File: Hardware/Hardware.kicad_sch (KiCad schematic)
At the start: 0 parts

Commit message: [Ajout] : Ajout du microcontrolleur STM32WB55RG utilisé dans le projet
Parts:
- added U1: STM32WB55RGVx, Package_DFN_QFN:QFN-68-1EP_8x8mm_P0.4mm_EP6.4x6.4mm, symbol MCU_ST_STM32WB:STM32WB55RGVx
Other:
- company: (none) -> PAR KAMDA JONATAN
- title: (none) -> SAFE ROOM SCHEMATIC
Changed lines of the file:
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@@
 	(generator_version "9.0")
 	(paper "A4")
+	(title_block
+		(title "SAFE ROOM SCHEMATIC")
+		(date "2026-05-06")
+		(rev "0.1")
+		(company "PAR KAMDA JONATAN")
+	)
+	(symbol
+		(lib_id "MCU_ST_STM32WB:STM32WB55RGVx")
+		(at 142.24 86.36 0)
+		(unit 1)
+		(exclude_from_sim no)
+		(in_bom yes)
+		(on_board yes)
+		(dnp no)
+		(fields_autoplaced yes)
+		(property "Reference" "U1"
+			(at 146.9233 134.62 0)
+			(effects
+				(font
+					(size 1.27 1.27)
+				)
+				(justify left)
+			)
+		)
+		(property "Value" "STM32WB55RGVx"
+			(at 146.9233 137.16 0)
+			(effects
+				(font
+					(size 1.27 1.27)
+				)
+				(justify left)
+			)
+		)
+		(property "Footprint" "Package_DFN_QFN:QFN-68-1EP_8x8mm_P0.4mm_EP6.4x6.4mm"
+			(at 121.92 132.08 0)
+			(effects
+				(font
+					(size 1.27 1.27)
+				)
+				(justify right)
+				(hide yes)
+			)
+		)
+		(property "Datasheet" "https://www.st.com/resource/en/datasheet/stm32wb55rg.pdf"
+			(at 142.24 86.36 0)
+			(effects
+				(font
+					(size 1.27 1.27)
+				)
+				(hide yes)
+			)
+		)
+		(property "Description" "STMicroelectronics Arm Cortex-M4 MCU, 1024KB flash, 256KB RAM, 64 MHz, 1.71-3.6V, 49 GPIO, VFQFPN68"
+			(at 142.24 86.36 0)
+			(effects
+				(font
+					(size 1.27 1.27)
+				)
+				(hide yes)
+			)
+		)
+		(pin "25"
+		)
+		(pin "32"
+		)
+		(pin "40"
+		)
+		(pin "58"
+		)
+		(pin "22"
+		)
+		(pin "8"
+		)
+		(pin "41"
+		)
+		(pin "2"
+		)
+		(pin "4"
+		)
+		(pin "26"
+		)
+		(pin "30"
+		)
+		(pin "36"
+		)
+		(pin "10"
+		)
+		(pin "45"
+		)
+		(pin "33"
+		)
+		(pin "55"
+		)
+		(pin "28"
+		)
+		(pin "43"
+		)
+		(pin "35"
+		)
+		(pin "1"
+		)
+		(pin "12"
+		)
+		(pin "61"
+		)
+		(pin "37"
+		)
+		(pin "9"
+		)
+		(pin "69"
+		)
+		(pin "24"
+		)
+		(pin "52"
+		)
+		(pin "19"
+		)
+		(pin "62"
+		)
+		(pin "23"
+		)
+		(pin "34"
+		)
+		(pin "63"
+		)
+		(pin "13"
+		)
+		(pin "11"
+		)
+		(pin "42"
+		)
+		(pin "18"
+		)
+		(pin "56"
+		)
+		(pin "44"
+		)
+		(pin "15"
+		)
+		(pin "57"
+		)
+		(pin "38"
+		)
+		(pin "27"
+		)
+		(pin "59"
+		)
+		(pin "60"
+		)
+		(pin "17"
+		)
+		(pin "68"
+		)
+		(pin "3"
+		)
+		(pin "5"
+		)
+		(pin "31"
+		)
+		(pin "50"
+		)
+		(pin "14"
+		)
+		(pin "16"
+		)
+		(pin "20"
+		)
+		(pin "21"
+		)
+		(pin "51"
+		)
+		(pin "54"
+		)
+		(pin "39"
+		)
+		(pin "64"
+		)
+		(pin "65"
+		)
+		(pin "66"
+		)
+		(pin "53"
+		)
+		(pin "67"
+		)
+		(pin "6"
+		)
+		(pin "7"
+		)
+		(pin "48"
+		)
+		(pin "49"
+		)
+		(pin "46"
+		)
+		(pin "29"
+		)
+		(pin "47"
+		)
+		(instances
+			(project ""
+				(path "/ba4846b8-7c71-441f-b11b-b34cbea60d05"
+					(reference "U1")
+					(unit 1)
+				)
+			)
+		)
+	)
 	(sheet_instances
 		(path "/"

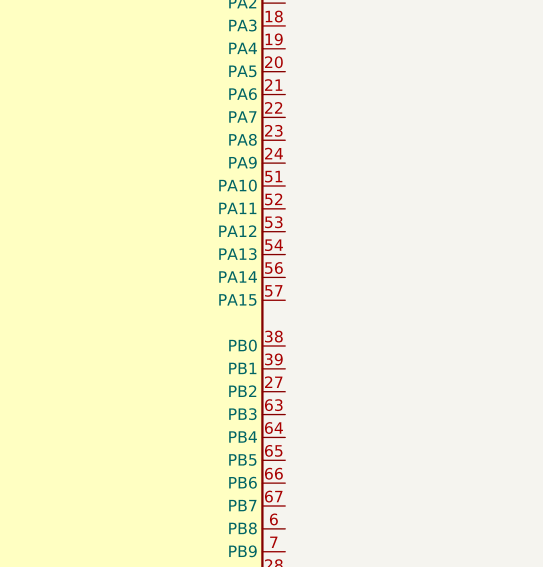
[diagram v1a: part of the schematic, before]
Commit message: [ST-LINK CONNEXION] : Ajout de la connexion ST-LINK pour téléverser le programme finale, il faut une connexion ST-LINK. La pin PA13 c'est pour la data ( SWDIO) La pin PA14 c'est pour l'horloge (SWCLK)
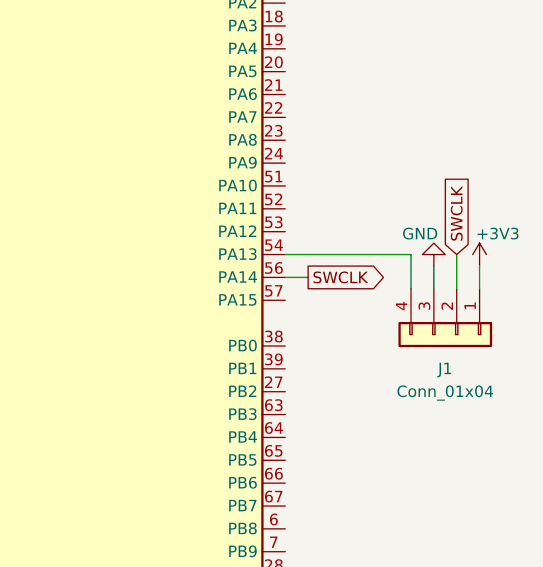
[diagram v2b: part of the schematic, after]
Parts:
- added J1: Conn_01x04, symbol Connector_Generic:Conn_01x04
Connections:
- net at U1.54 (PA13): now also J1.4 (Pin_4)
- net SWCLK: now reaches U1.56 (PA14)
- net SWCLK: now also J1.2 (Pin_2)
- new net +3V3: J1.1 (Pin_1)
- new net GND: J1.3 (Pin_3)

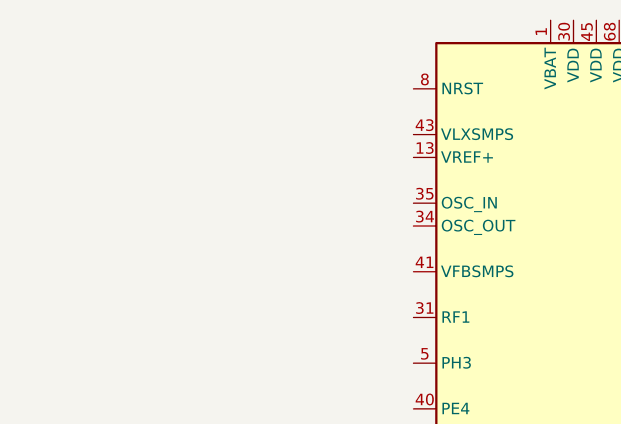
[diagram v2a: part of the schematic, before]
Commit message: [RESET]: Ajout du bouton reset et de la capacité pour filtrer les oscillations du bouton
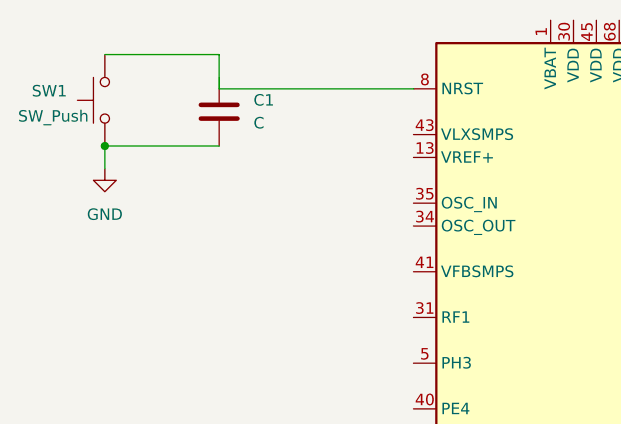
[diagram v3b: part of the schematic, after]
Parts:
- added C1: C, symbol Device:C
- added SW1: SW_Push, symbol Switch:SW_Push
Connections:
- net GND: now also C1.2, SW1.1
- net at U1.8 (NRST): now also SW1.2

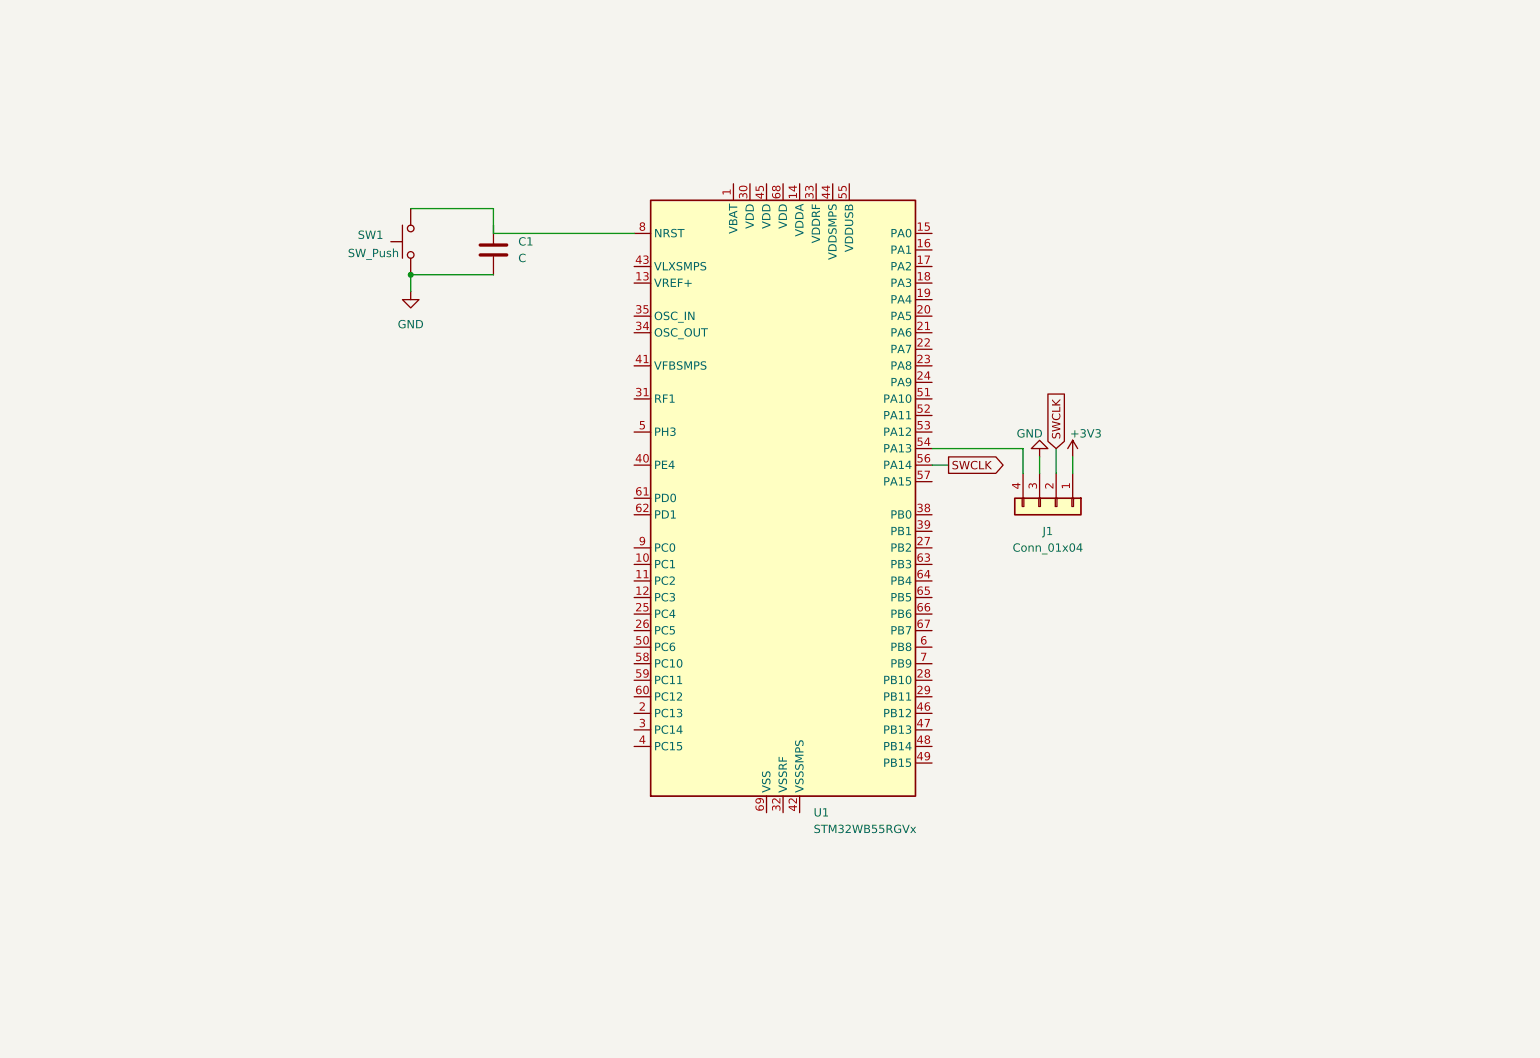
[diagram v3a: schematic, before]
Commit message: [PARTIE ALIMENTATION] : Mise en place des condensateur de découplage pour les alimentations VDD, VBAT, VDDA, VREF, VDDRF et VDSMPS. Les consignes des valeurs des condensateur de découplage sont données dans le manuelle de ST.
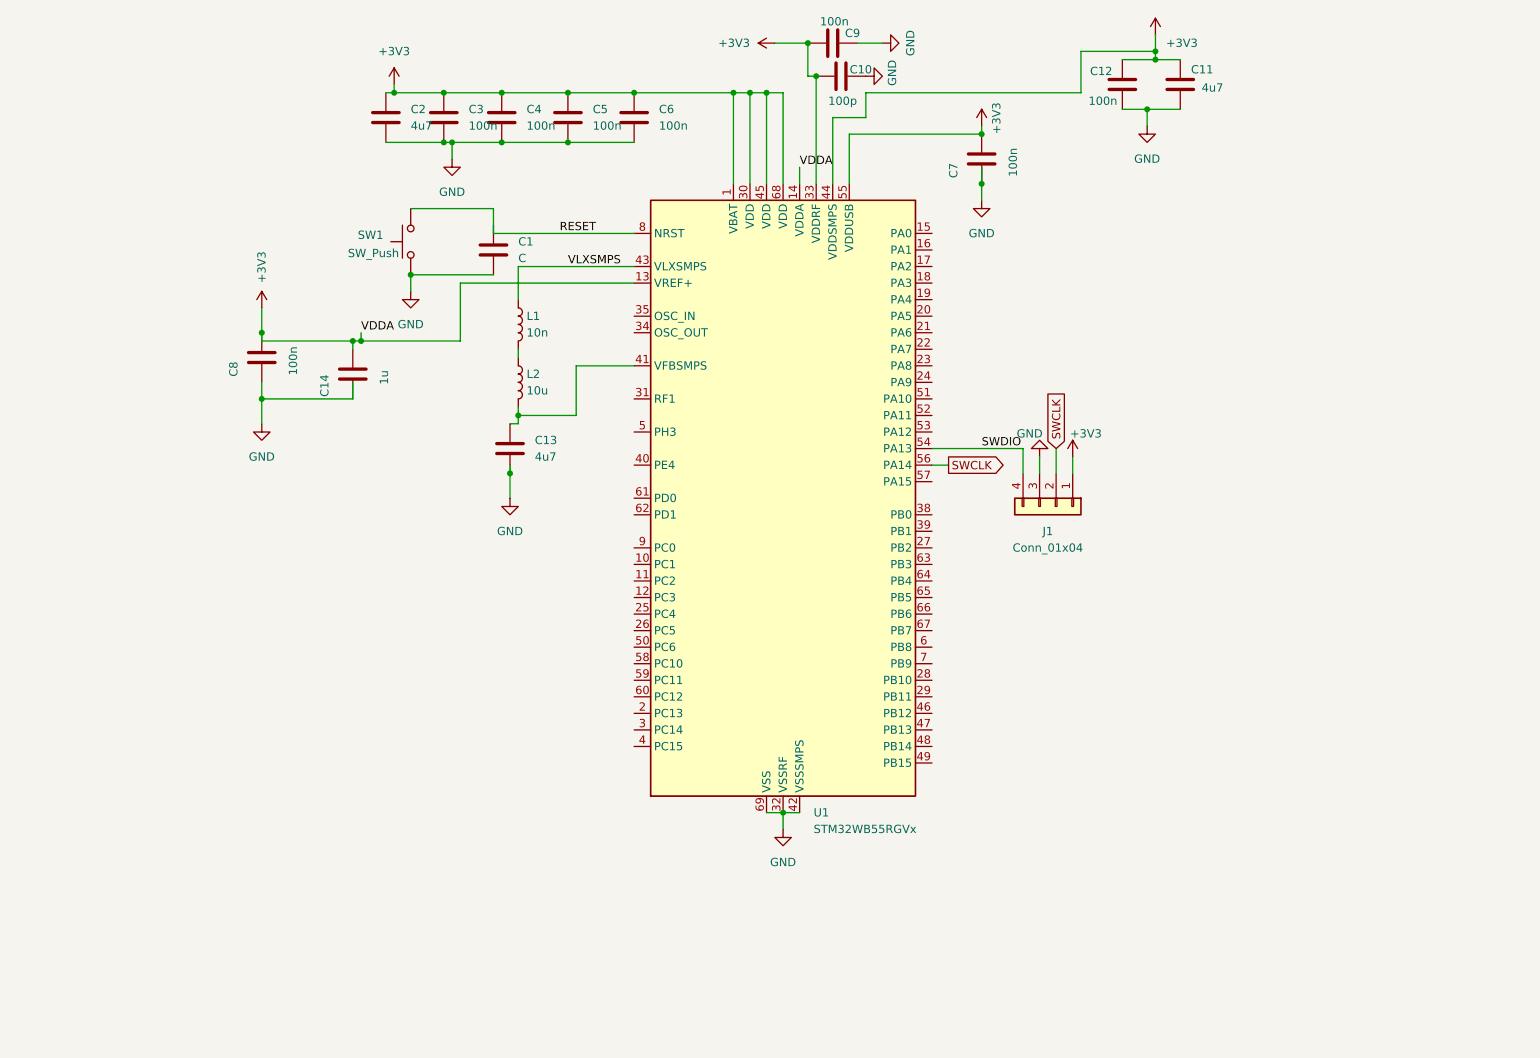
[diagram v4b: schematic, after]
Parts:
- added C10: 100p, symbol Device:C
- added C11, C13, C2: 4u7, symbol Device:C
- added C12, C3, C4, C5, C6, C7, C8, C9: 100n, symbol Device:C
- added C14: 1u, symbol Device:C
- added L1: 10n, symbol Device:L
- added L2: 10u, symbol Device:L
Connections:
- net +3V3: now also U1.1 (VBAT), U1.13 (VREF+), U1.14 (VDDA), U1.30 (VDD), U1.33 (VDDRF), U1.44 (VDDSMPS), U1.45 (VDD), U1.55 (VDDUSB), U1.68 (VDD), C10.2, C11.1, C12.1, C14.2, C2.1, C3.1, C4.1, C5.1, C6.1, C7.2, C8.2, C9.2
- net GND: now also U1.32 (VSSRF), U1.42 (VSSSMPS), U1.69 (VSS), C10.1, C11.2, C12.2, C13.2, C14.1, C2.2, C3.2, C4.2, C5.2, C6.2, C7.1, C8.1, C9.1
- net SWDIO: now reaches J1.4 (Pin_4), U1.54 (PA13)
- net at U1.41 (VFBSMPS): now also C13.1, L2.2
- net VLXSMPS: now reaches U1.43 (VLXSMPS)
- net VLXSMPS: now also L1.1
- net RESET: now reaches SW1.2, U1.8 (NRST)
- new net: L1.2, L2.1

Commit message: [Ajout des montages d'Oscillateurs et du Montage RF] Pour concevoir les montages d'oscillateur on utilise le document applicative de ST. Pour concevoir le montage RF, on a également utilisé le meme document. Il s'agit du document AN5165, page utilisé 15/62.
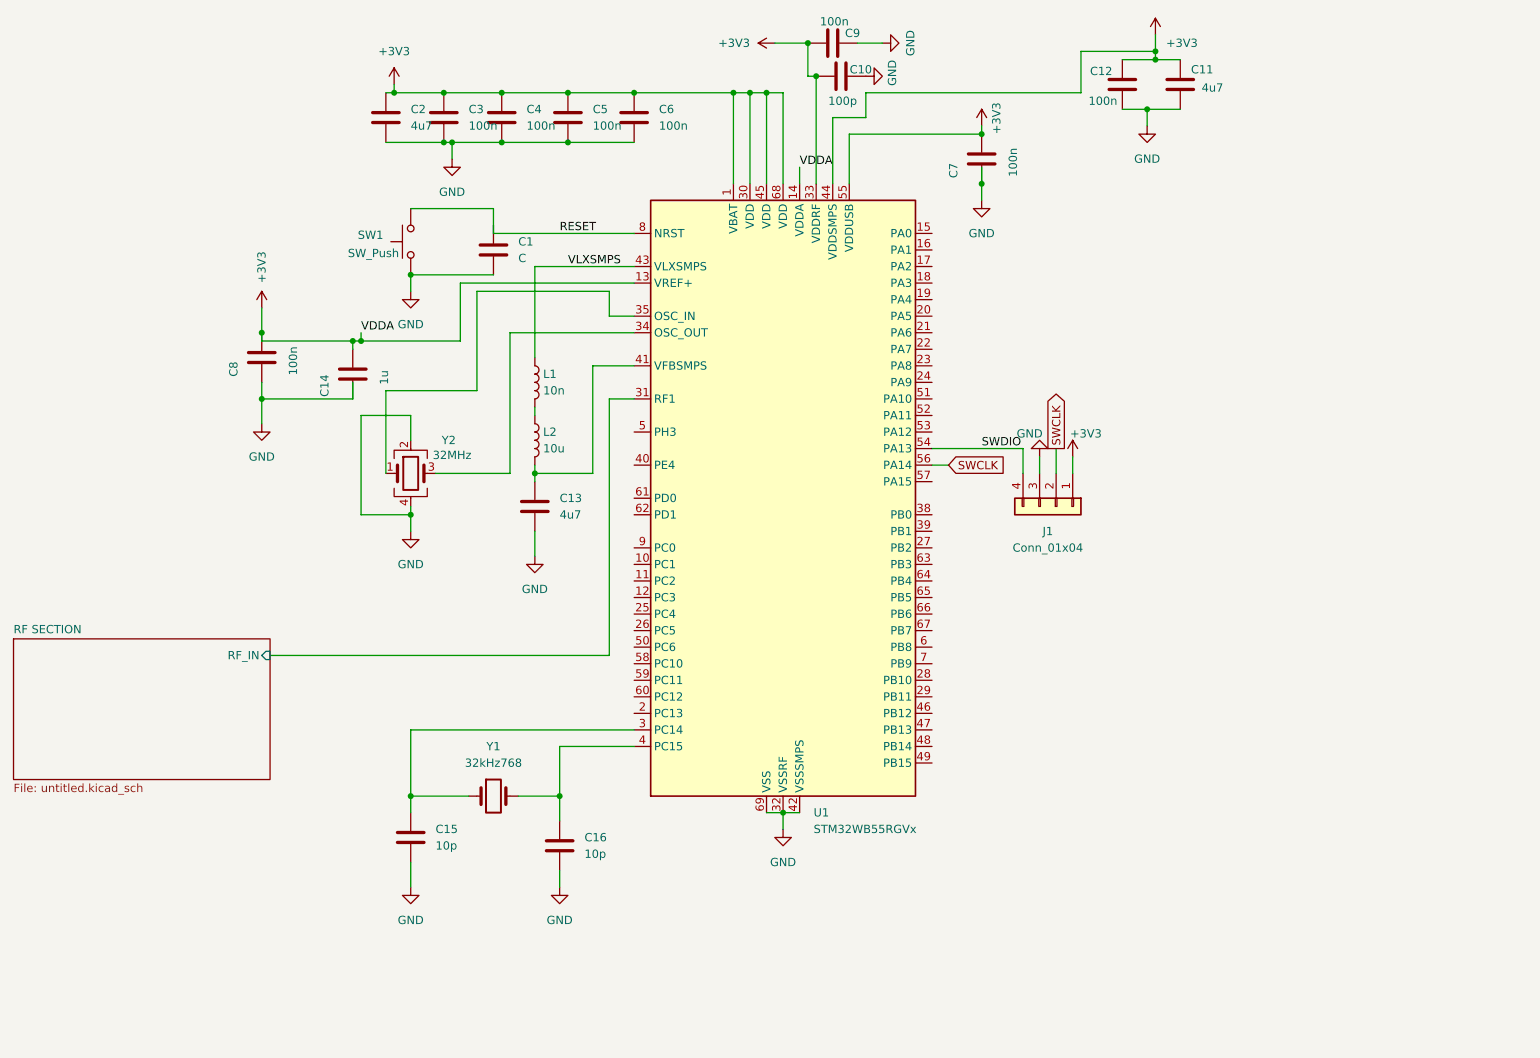
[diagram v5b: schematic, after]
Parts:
- added C15, C16: 10p, symbol Device:C
- added Y1: 32kHz768, symbol Device:Crystal
- added Y2: 32MHz, symbol Device:Crystal_GND24
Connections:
- net GND: now also C15.2, C16.2, Y2.2, Y2.4
- net at U1.3 (PC14): now also C15.1, Y1.1
- net RF SECTION/RF_IN: now reaches U1.31 (RF1)
- net at U1.34 (OSC_OUT): now also Y2.3
- net at U1.35 (OSC_IN): now also Y2.1
- net at U1.4 (PC15): now also C16.1, Y1.2
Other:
- added sheet RF SECTION (untitled.kicad_sch)
- moved on the sheet: C13, L1, L2
